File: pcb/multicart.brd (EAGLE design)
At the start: 67.3 x 87 mm, 28 parts, among them IC1 27C64-27C080, IC2 74HCT373N, IC3 74HCT08N, Q1 BS170

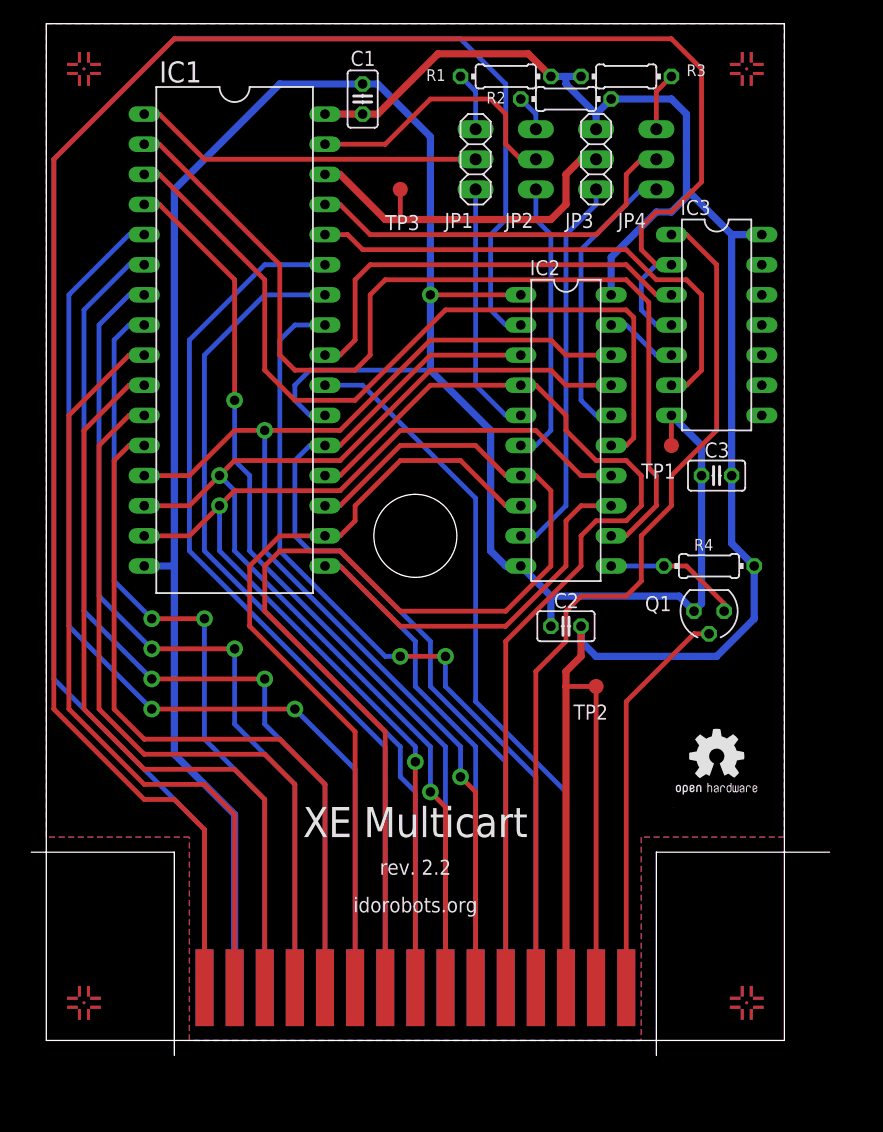
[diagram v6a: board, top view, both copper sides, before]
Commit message: Adjusted trace widths to make home etching easier.
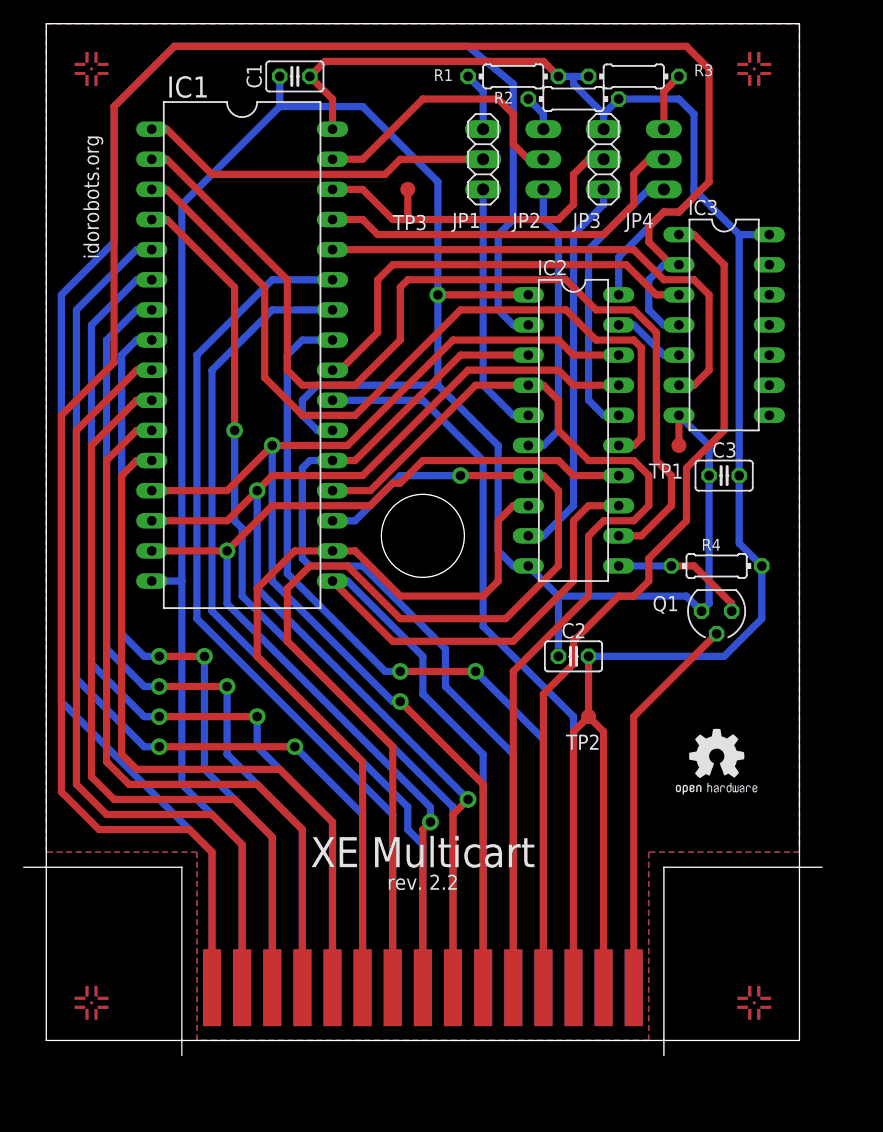
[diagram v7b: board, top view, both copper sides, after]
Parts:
- moved C1 6.02 mm to (21.0, 81.3), turned to 180 degrees
- moved C2 2.62 mm to (44.5, 32.4)
- moved TP2 2.62 mm to (45.7, 27.3)
- moved IC1 1.42 mm to (16.5, 57.8)
- moved IC2 0.64 mm to (44.5, 51.4)
- moved JP3 0.64 mm to (47.0, 74.3)
- moved R2 0.64 mm to (44.5, 79.4)
- moved TP1 0.64 mm to (53.3, 50.2)
- moved J1 0.64 mm to (31.8, 0.64)
- moved TP3 0.64 mm to (30.5, 71.8)
- moved U$1 0.64 mm to (3.81, 81.9)
- moved U$4 0.64 mm to (3.81, 81.9)
- moved U$5 0.64 mm to (3.81, 3.17)
- moved U$6 0.64 mm to (3.81, 3.17)
- moved C3 0.63 mm to (57.1, 47.6)
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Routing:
- net D5: track 97.2 -> 92.2 mm, vias 0 -> 1
- net D2: track 92.1 -> 87.2 mm
- net VCC: track 175.0 -> 171.4 mm
- net N$19: track 166.3 -> 168.4 mm
- net N$18: track 74.4 -> 72.9 mm
- net A10: track 61.1 -> 62.4 mm
- net A12: track 77.3 -> 76.0 mm
- net D6: track 83.1 -> 84.4 mm
- net A8: track 75.5 -> 74.2 mm
- net A5: track 71.7 -> 70.4 mm
- net A9: track 73.0 -> 71.7 mm
- net A6: track 77.8 -> 76.5 mm
- net D4: track 68.1 -> 69.2 mm
- net N$3: track 69.4 -> 68.4 mm
- net A3: track 65.5 -> 66.4 mm
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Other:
- outline, holes or cut-outs redrawn

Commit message: Optimized the design.
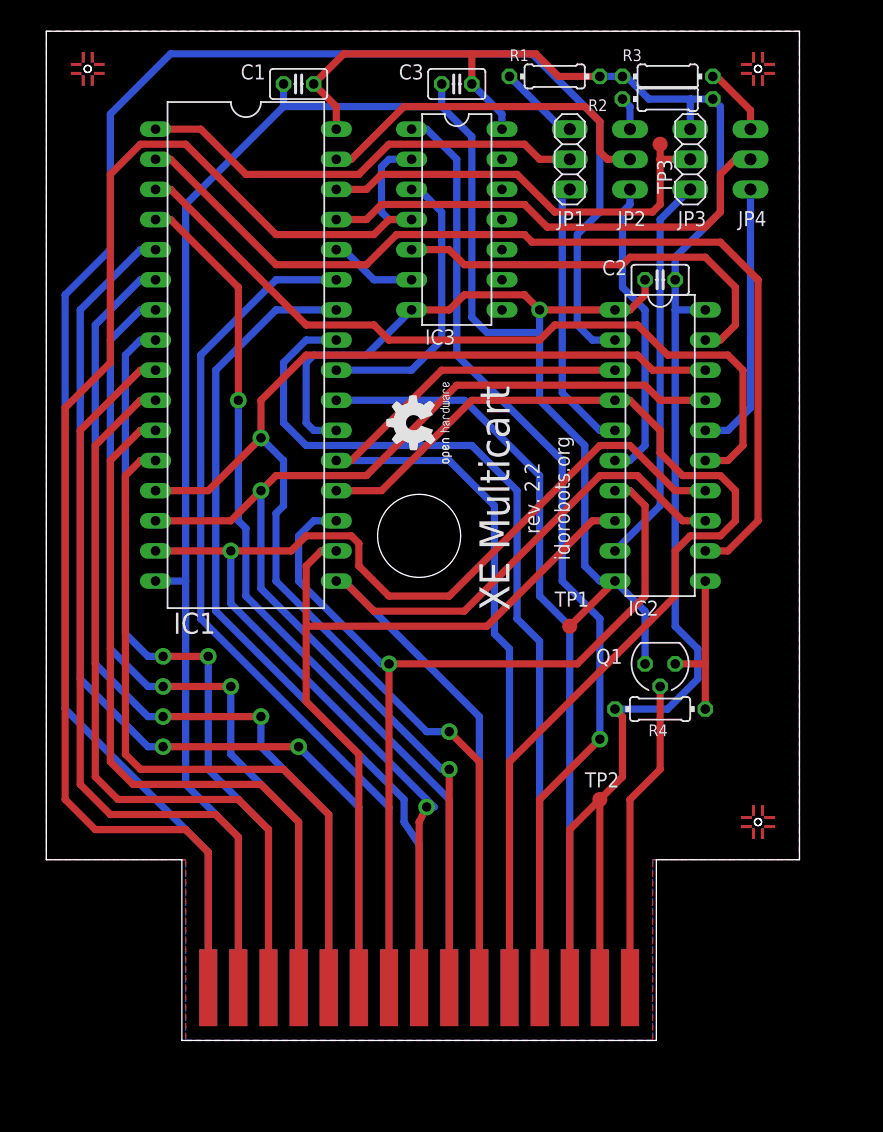
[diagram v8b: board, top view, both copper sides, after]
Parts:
- removed U$7, U$8: (no value), marks:PASSER-CIRCLE
- U$1, U$2, U$3, U$4, U$5, U$6: device marks:PASSER-CIRCLE -> marks:PASSER-HOLE
- moved U$5 58.2 mm to (60.0, 18.4), flipped to the top, turned to 0 degrees
- moved U$6 58.2 mm to (60.0, 18.4), flipped to the bottom, turned to 0 degrees
- moved U$2 56.2 mm to (3.49, 81.9), flipped to the bottom
- moved U$4 56.2 mm to (60.0, 81.9), flipped to the top, turned to 0 degrees
- moved C3 40.0 mm to (34.6, 80.6)
- moved GOLD_ORB_SM1 33.5 mm to (35.2, 48.3), turned to 90 degrees
- moved C2 32.6 mm to (51.8, 64.1)
- moved IC3 24.2 mm to (34.6, 69.2)
- moved TP3 21.6 mm to (51.8, 75.6)
- moved TP1 17.8 mm to (44.1, 34.9)
- moved R4 13.0 mm to (51.8, 27.9), turned to 0 degrees
- moved R2 7.94 mm to (52.4, 79.4)
- moved IC2 7.41 mm to (51.8, 50.2)
- moved JP1 7.30 mm to (44.1, 74.3)
- moved JP2 7.30 mm to (49.2, 74.3)
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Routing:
- net N$19: track 168.4 -> 119.2 mm
- net N$21: track 42.7 -> 7.40 mm
- net N$1: track 6.13 -> 35.4 mm
- net VCC: track 171.4 -> 154.4 mm
- net D2: track 87.2 -> 101.7 mm
- net N$27: track 36.5 -> 24.1 mm
- net D5: track 92.2 -> 80.0 mm
- net D0: track 98.6 -> 109.1 mm
- net N$18: track 72.9 -> 81.8 mm, vias 0 -> 1
- net N$13: track 30.0 -> 38.1 mm
- net D6: track 84.4 -> 92.4 mm
- net N$15: track 32.6 -> 40.5 mm
- net N$12: track 30.0 -> 37.0 mm
- net N$22: track 140.9 -> 147.6 mm
- net N$10: track 23.5 -> 29.9 mm
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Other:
- board size 67.3 x 87 mm -> 63.5 x 85.1 mm
